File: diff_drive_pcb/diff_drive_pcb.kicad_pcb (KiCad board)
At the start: 2 copper layers, 110 x 110 mm, 34 parts, among them J1 P_M1, J10 12V_IN, J11 Motor_Break_SW, J12 POWER_SW, J2 Encoder_M1, J3 P_M2, J4 Encoder_M2, J5 P_M3, J6 Encoder_M3, J7 P_M4, J8 Encoder_M4, J9 5V_IN, Q2 IRLZ24, U1 Motor Driver 1, U2 Motor Driver 2, U3 Teensy4.1, U4 TOF_front_left, U5 Tof_back_left, U6 Tof_front_right, U7 Tof_back_right, U8 MPU9250

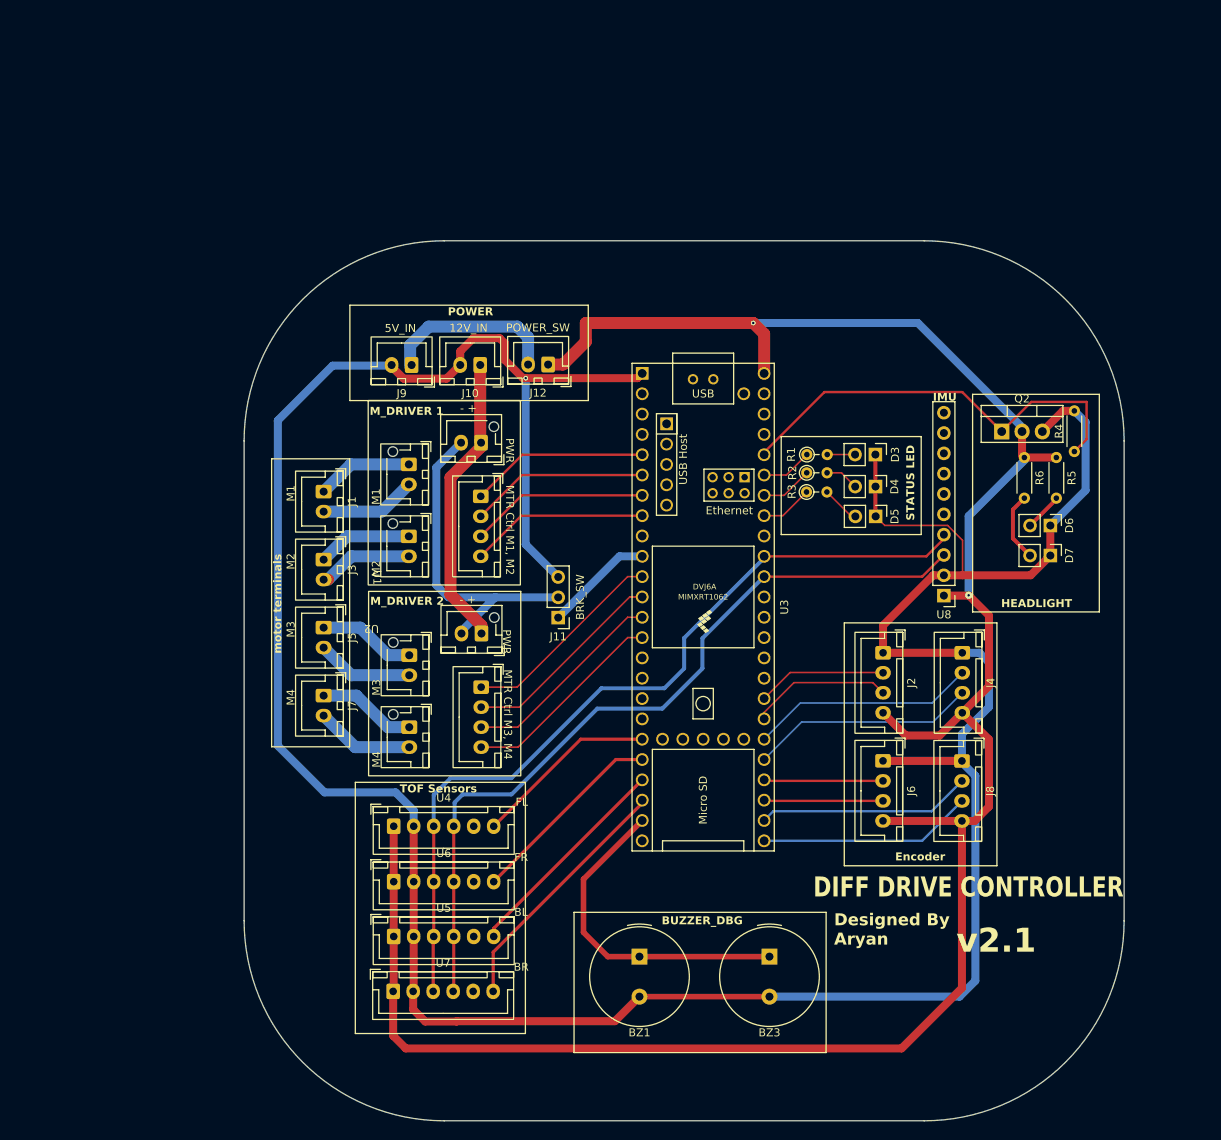
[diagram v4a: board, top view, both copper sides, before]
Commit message: V2.2 changes to power system
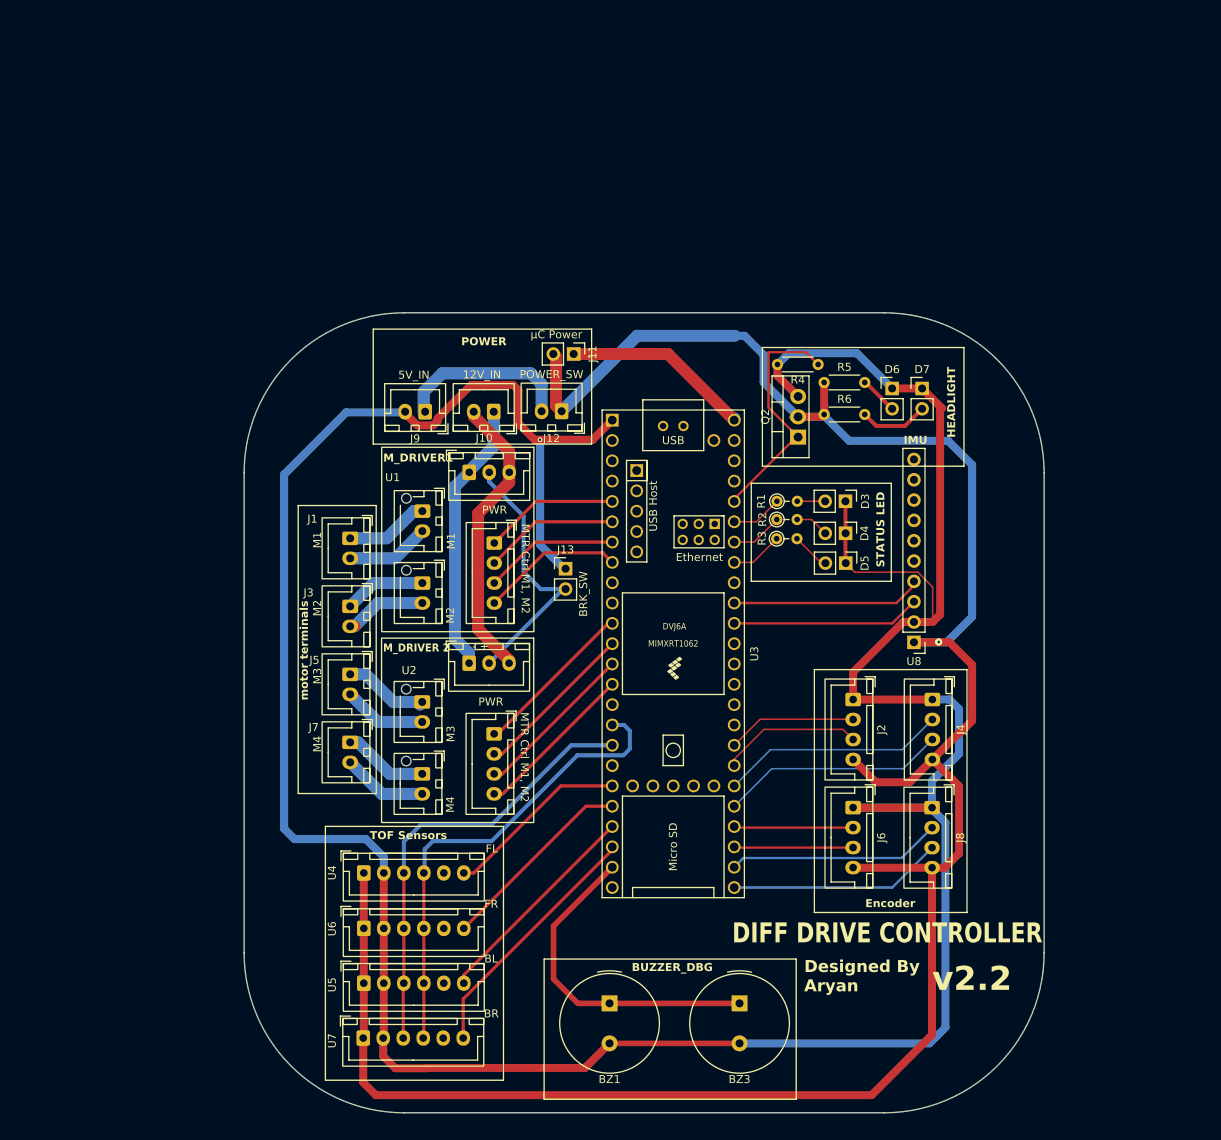
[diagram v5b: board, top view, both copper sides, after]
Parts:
- added J13: Motor_Break_SW, Connector_PinHeader_2.54mm:PinHeader_1x02_P2.54mm_Vertical, F.Cu at (140.2, 91.0)
- J11: footprint Connector_PinHeader_2.54mm:PinHeader_1x03_P2.54mm_Vertical -> Connector_PinHeader_2.54mm:PinHeader_1x02_P2.54mm_Vertical
- moved R4 33.8 mm to (171.8, 65.5), turned to 180 degrees
- moved J11 33.0 mm to (141.2, 64.2), turned to -90 degrees
- moved R5 30.5 mm to (172.5, 67.7), turned to 0 degrees
- moved D7 26.3 mm to (184.8, 68.5), turned to 0 degrees
- moved D6 26.2 mm to (181.0, 68.5), turned to 0 degrees
- moved R6 25.6 mm to (172.5, 71.7), turned to 0 degrees
- moved Q2 25.5 mm to (169.2, 74.5), turned to 90 degrees
- moved D3 6.93 mm to (175.2, 82.6)
- moved D4 6.93 mm to (175.2, 86.6)
- moved J2 6.93 mm to (176.1, 107.3)
- moved J4 6.93 mm to (186.0, 107.3)
- moved R1 6.93 mm to (166.6, 82.6)
- moved U4 6.93 mm to (115.0, 129.0)
- moved U5 6.93 mm to (115.0, 142.8)
- moved U8 6.93 mm to (183.7, 100.2)
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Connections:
- J10 pad 2: GND -> GND1
- J11 pad 1: /MD_stby -> uC_pwr
- J11 pad 2: /Brk_sw -> +5V
- U3 pad 10: /MD_stby -> unconnected-(U3-8_TX2_IN1-Pad10)
- U3 pad 16: unconnected-(U3-24_A10_TX6_SCL2-Pad16) -> TOF_SCL
- U3 pad 17: unconnected-(U3-25_A11_RX6_SDA2-Pad17) -> TOF_SDA
- U3 pad 48: +5V -> uC_pwr
- U4 pad 3: MPU_SDA -> TOF_SDA
- U4 pad 4: MPU_SCL -> TOF_SCL
- U5 pad 3: MPU_SDA -> TOF_SDA
- U5 pad 4: MPU_SCL -> TOF_SCL
- U6 pad 3: MPU_SDA -> TOF_SDA
- U6 pad 4: MPU_SCL -> TOF_SCL
- U7 pad 3: MPU_SDA -> TOF_SDA
- U7 pad 4: MPU_SCL -> TOF_SCL
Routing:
- net MPU_SDA: track 104.7 -> 24.1 mm
- net MPU_SCL: track 99.9 -> 23.6 mm
- net TOF_SCL: track 0.00 -> 59.3 mm
- net TOF_SDA: track 0.00 -> 55.6 mm
- net GND1: track 0.00 -> 37.6 mm
- net HEADLIGHTS: track 54.3 -> 30.1 mm
- net uC_pwr: track 0.00 -> 23.9 mm
- net /MD_stby: track 13.7 -> 0.00 mm
- net /Brk_sw: track 41.2 -> 33.9 mm
- net +5V: track 284.7 -> 291.5 mm, vias 2 -> 1
- net M2_ctrl_A: track 22.3 -> 16.9 mm
- net M1_ctrl_B: track 22.3 -> 16.9 mm
- net M1_ctrl_A: track 22.3 -> 16.9 mm
- net M4_ctrl_B: track 25.8 -> 20.4 mm
- net M4_ctrl_A: track 25.8 -> 20.5 mm
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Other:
- board size 110 x 110 mm -> 100 x 100 mm
- board text added: "M_DRIVER1"
- board text added: "v2.2"
- board text added: "μC Power"
- board text removed: "M_DRIVER 1"
- board text removed: "v2.1"

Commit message: Generated gerb files for v2.2
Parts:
- removed U2: Motor Driver 2, MDD3A:MDD3A
